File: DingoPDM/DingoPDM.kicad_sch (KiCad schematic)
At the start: 6 parts

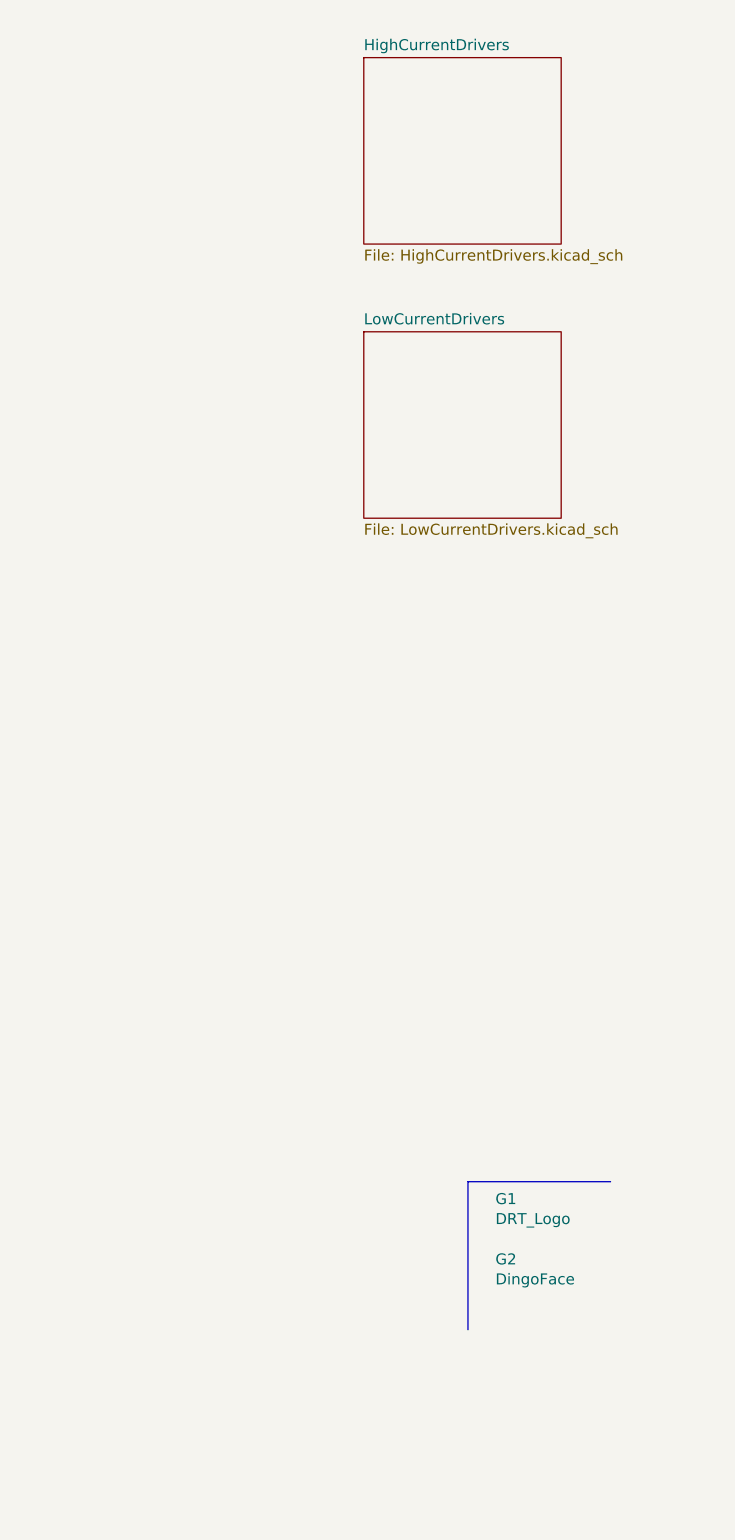
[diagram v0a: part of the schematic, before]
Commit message: Changed schematic sheet size to letter
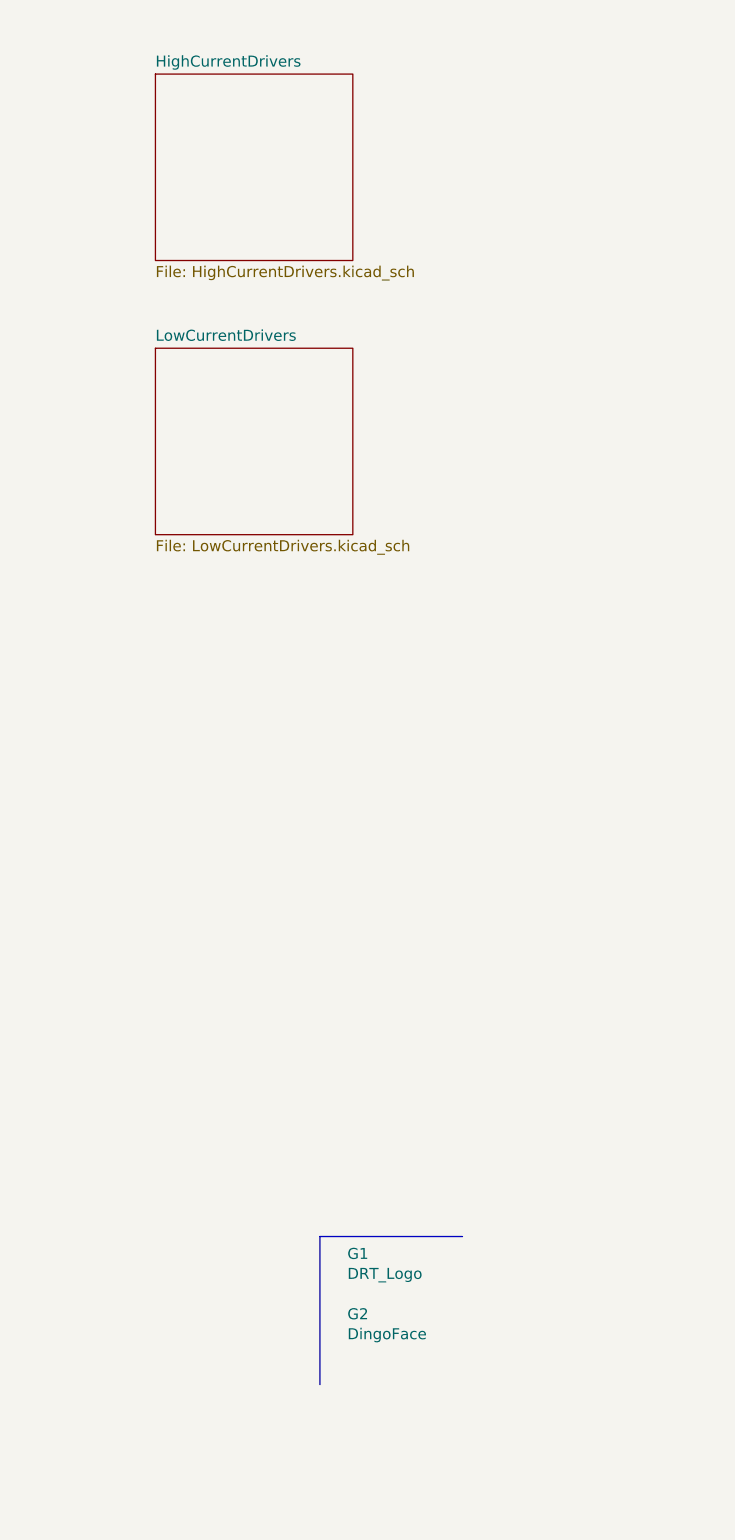
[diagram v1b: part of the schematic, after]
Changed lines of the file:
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@@
 (kicad_sch (version 20230121) (generator eeschema)
-  (paper "A4")
+  (paper "USLetter")
   (title_block
     (title "Dingo_PDM")
-    (date "2023-02-23")
+    (date "2023-04-01")
     (rev "v5")
     (comment 3 "github.com/corygrant")
@@
     (stroke (width 0) (type default))
   )
-  (polyline (pts (xy 267.335 147.955) (xy 283.845 147.955))
+  (polyline (pts (xy 250.19 154.305) (xy 266.7 154.305))
     (stroke (width 0) (type default))
   )
@@
     (stroke (width 0) (type default))
   )
-  (polyline (pts (xy 267.335 165.1) (xy 267.335 147.955))
+  (polyline (pts (xy 250.19 171.45) (xy 250.19 154.305))
     (stroke (width 0) (type default))
   )
@@
     )
   )
-  (symbol (lib_id "DRT_Logo:DRT_Logo") (at 269.875 151.13 0) (unit 1)
-    (in_bom yes) (on_board yes) (dnp no)
-    (property "Reference" "G1" (at 270.51 149.9616 0)
-      (effects (font (size 1.27 1.27)) (justify left))
-    )
-    (property "Value" "DRT_Logo" (at 270.51 152.273 0)
-      (effects (font (size 1.27 1.27)) (justify left))
-    )
-    (property "Footprint" "DRTLogo:DRTLogo" (at 269.875 151.13 0)
-      (effects (font (size 1.27 1.27)) hide)
-    )
-    (property "Datasheet" "" (at 269.875 151.13 0)
+  (symbol (lib_id "DRT_Logo:DRT_Logo") (at 252.73 157.48 0) (unit 1)
+    (in_bom yes) (on_board yes) (dnp no)
+    (property "Reference" "G1" (at 253.365 156.3116 0)
+      (effects (font (size 1.27 1.27)) (justify left))
+    )
+    (property "Value" "DRT_Logo" (at 253.365 158.623 0)
+      (effects (font (size 1.27 1.27)) (justify left))
+    )
+    (property "Footprint" "DRTLogo:DRTLogo" (at 252.73 157.48 0)
+      (effects (font (size 1.27 1.27)) hide)
+    )
+    (property "Datasheet" "" (at 252.73 157.48 0)
       (effects (font (size 1.27 1.27)) hide)
     )
@@
     )
   )
-  (symbol (lib_id "DRT_Logo:DRT_Logo") (at 269.875 158.115 0) (unit 1)
-    (in_bom yes) (on_board yes) (dnp no)
-    (property "Reference" "G2" (at 270.51 156.9466 0)
-      (effects (font (size 1.27 1.27)) (justify left))
-    )
-    (property "Value" "DingoFace" (at 270.51 159.258 0)
-      (effects (font (size 1.27 1.27)) (justify left))
-    )
-    (property "Footprint" "DRTLogo:DingoFaceNoFill" (at 269.875 158.115 0)
-      (effects (font (size 1.27 1.27)) hide)
-    )
-    (property "Datasheet" "" (at 269.875 158.115 0)
+  (symbol (lib_id "DRT_Logo:DRT_Logo") (at 252.73 164.465 0) (unit 1)
+    (in_bom yes) (on_board yes) (dnp no)
+    (property "Reference" "G2" (at 253.365 163.2966 0)
+      (effects (font (size 1.27 1.27)) (justify left))
+    )
+    (property "Value" "DingoFace" (at 253.365 165.608 0)
+      (effects (font (size 1.27 1.27)) (justify left))
+    )
+    (property "Footprint" "DRTLogo:DingoFaceNoFill" (at 252.73 164.465 0)
+      (effects (font (size 1.27 1.27)) hide)
+    )
+    (property "Datasheet" "" (at 252.73 164.465 0)
       (effects (font (size 1.27 1.27)) hide)
     )
@@
     )
   )
-  (sheet (at 255.27 17.78) (size 22.86 21.59) (fields_autoplaced)
+  (sheet (at 231.14 19.685) (size 22.86 21.59) (fields_autoplaced)
     (stroke (width 0) (type solid))
     (fill (color 0 0 0 0.0000))
-    (property "Sheetname" "HighCurrentDrivers" (at 255.27 17.0684 0)
+    (property "Sheetname" "HighCurrentDrivers" (at 231.14 18.9734 0)
       (effects (font (size 1.27 1.27)) (justify left bottom))
     )
-    (property "Sheetfile" "HighCurrentDrivers.kicad_sch" (at 255.27 39.9546 0)
+    (property "Sheetfile" "HighCurrentDrivers.kicad_sch" (at 231.14 41.8596 0)
       (effects (font (size 1.27 1.27)) (justify left top))
     )
@@
     )
   )
-  (sheet (at 255.27 49.53) (size 22.86 21.59) (fields_autoplaced)
+  (sheet (at 231.14 51.435) (size 22.86 21.59) (fields_autoplaced)
     (stroke (width 0) (type solid))
     (fill (color 0 0 0 0.0000))
-    (property "Sheetname" "LowCurrentDrivers" (at 255.27 48.8184 0)
+    (property "Sheetname" "LowCurrentDrivers" (at 231.14 50.7234 0)
       (effects (font (size 1.27 1.27)) (justify left bottom))
     )
-    (property "Sheetfile" "LowCurrentDrivers.kicad_sch" (at 255.27 71.7046 0)
+    (property "Sheetfile" "LowCurrentDrivers.kicad_sch" (at 231.14 73.6096 0)
       (effects (font (size 1.27 1.27)) (justify left top))
     )

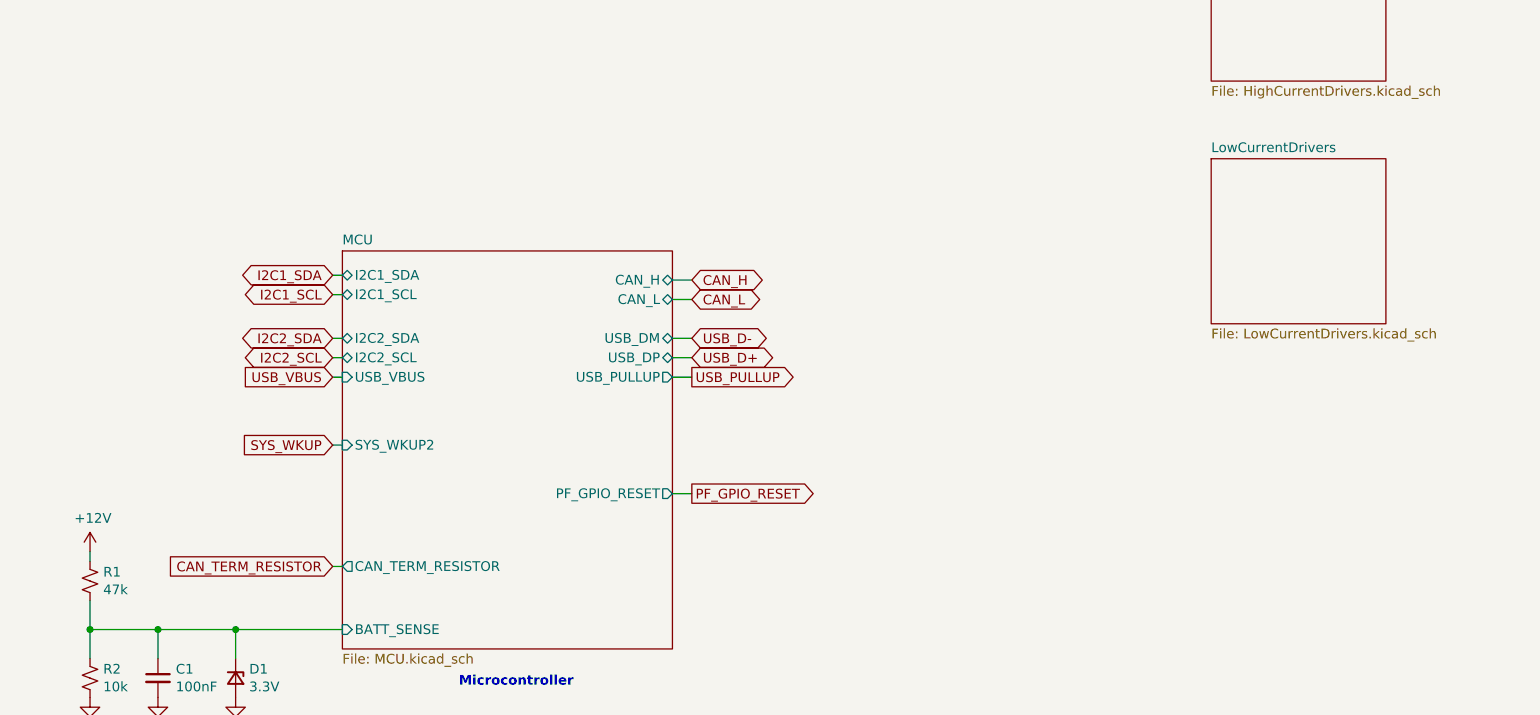
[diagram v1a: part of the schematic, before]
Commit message: Redesigned to a smaller unit
4x high current, 2x med current, 4x low current, 2x digital inputs
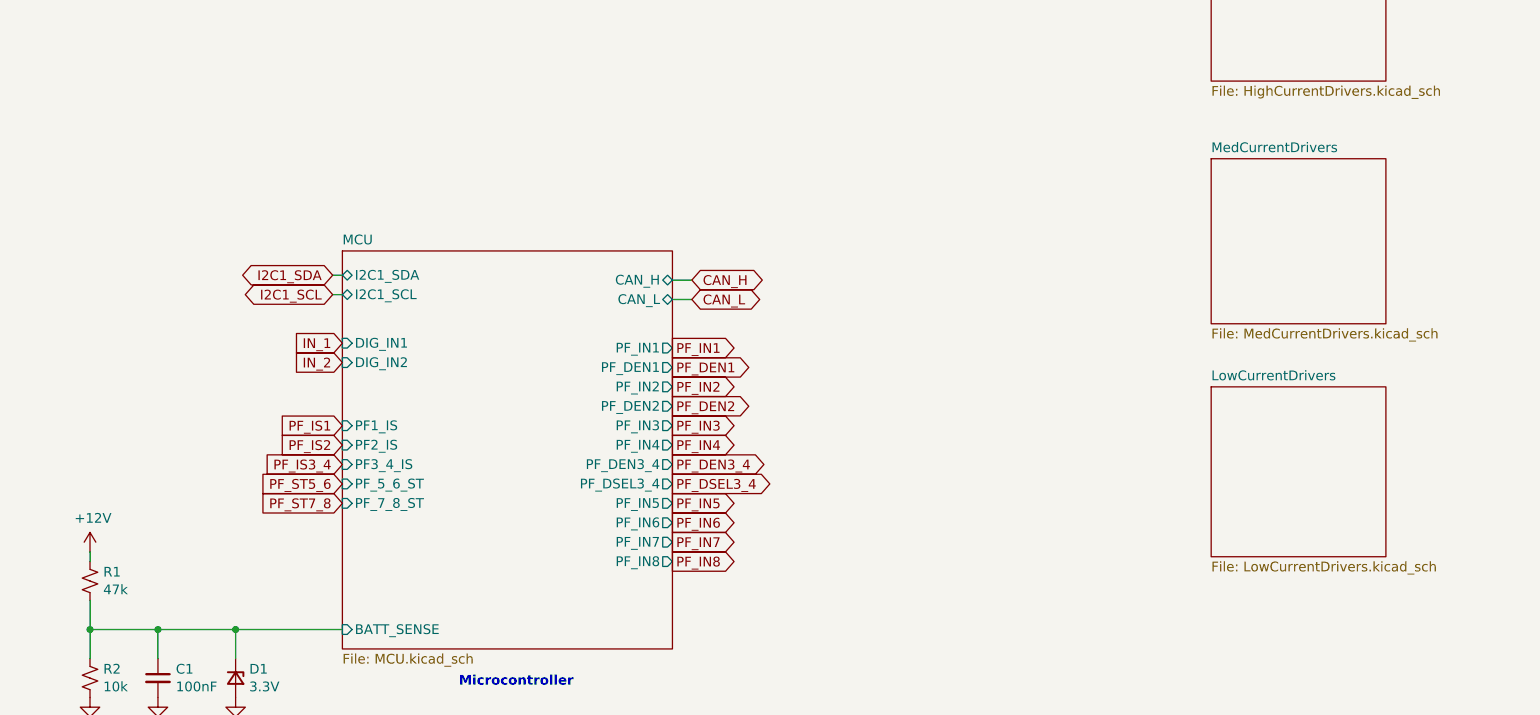
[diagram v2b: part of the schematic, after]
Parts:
- C1: LCSC (none) -> C49678
- R2: LCSC (none) -> C17414
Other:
- added sheet MedCurrentDrivers (MedCurrentDrivers.kicad_sch)
- sheet MCU ports: added DIG_IN1, DIG_IN2, PF1_IS, PF2_IS, PF3_4_IS, PF_5_6_ST, PF_7_8_ST, PF_DEN1, PF_DEN2, PF_DEN3_4, PF_DSEL3_4, PF_IN1, PF_IN2, PF_IN3, PF_IN4, PF_IN5, PF_IN6, PF_IN7, PF_IN8; removed CAN_TERM_RESISTOR, I2C2_SCL, I2C2_SDA, PF_GPIO_RESET, SYS_WKUP2, USB_DM, USB_DP, USB_PULLUP, USB_VBUS

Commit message: Added documentation, finished and cleaned design
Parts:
- D1: LCSC (none) -> C177016
- R1: LCSC (none) -> C327035
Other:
- note added: "V6 -Drastically simplied design -Changed to 2x high power outputs, 2x med power outputs, and 4x low power outputs -Changed to 2x digital inputs -Removed USB -Removed SPI Flash -Removed VBAT super cap -Removed I2C GPIO -Removed I2C ADC -Removed LEDs and I2C driver -Changed to single Deutsch DT -Added a RedCube for ground -Removed power on/sleep input -Removed CAN terminating resistor switch -Remov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"
- note removed: "V5 -Changed ADS1015 to MAX11613EUA+T due to supply issues -Changed PCB to match JLCPCB 2oz rules -Changed ON_SW input to 12V switched -Switched to TagConnect TC2030 -Changed pin positions of GND, IN1, IN2"
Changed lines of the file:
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@@
   (title_block
     (title "Dingo_PDM")
-    (date "2023-07-25")
+    (date "2023-07-28")
     (rev "v6")
     (comment 3 "github.com/corygrant")
@@
     (effects (font (size 1.27 1.27) (thickness 0.254) bold) (justify left bottom))
   )
-  (text "V5\n-Changed ADS1015 to MAX11613EUA+T due to supply issues\n-Changed PCB to match JLCPCB 2oz rules\n-Changed ON_SW input to 12V switched\n-Switched to TagConnect TC2030\n-Changed pin positions of GND, IN1, IN2"
+  (text "V6\n-Drastically simplied design\n-Changed to 2x high power outputs, 2x med power outputs, and 4x low power outputs\n-Changed to 2x digital inputs\n-Removed USB\n-Removed SPI Flash\n-Removed VBAT super cap\n-Removed I2C GPIO\n-Removed I2C ADC\n-Removed LEDs and I2C driver\n-Changed to single Deutsch DT\n-Added a RedCube for ground\n-Removed power on/sleep input\n-Removed CAN terminating resistor switch\n-Removed input power switch"
     (at 86.995 189.23 0)
     (effects (font (size 1.27 1.27)) (justify left bottom))
@@
       (effects (font (size 1.27 1.27)) hide)
     )
-    (property "LCSC" "" (at 84.455 106.68 0)
+    (property "LCSC" "C327035" (at 84.455 106.68 0)
       (effects (font (size 1.27 1.27)) hide)
     )
@@
       (effects (font (size 1.27 1.27)) hide)
     )
-    (property "LCSC" "" (at 103.505 119.38 0)
-      (effects (font (size 1.27 1.27)) hide)
-    )
+    (property "LCSC" "C177016" (at 103.505 119.38 0)
+      (effects (font (size 1.27 1.27)) hide)
+    )
